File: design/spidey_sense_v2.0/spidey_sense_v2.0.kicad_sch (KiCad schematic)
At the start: 13 parts, among them J1 Input_Screw_Terminal, J2 Output_Screw_Terminal, J3 Thermocouple_Terminal, J4 Thermocouple_Terminal, J5 Thermocouple_Terminal, J6 Thermocouple_Terminal, U1 LT1025, U2 LTC1983-5

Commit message: Updated footprints
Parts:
- U1: footprint SamacSys_Parts:SOIC127P599X175-8N -> Package_SO:SOP-8_3.9x4.9mm_P1.27mm
- U2: footprint SamacSys_Parts:SOT95P280X100-6N -> Package_SO:TSOP-6_1.65x3.05mm_P0.95mm
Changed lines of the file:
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@@
     (property "Reference" "U1" (id 0) (at 80.01 70.739 0))
     (property "Value" "LT1025" (id 1) (at 80.01 73.0504 0))
-    (property "Footprint" "SamacSys_Parts:SOIC127P599X175-8N" (id 2) (at 63.5 73.66 0)
+    (property "Footprint" "Package_SO:SOP-8_3.9x4.9mm_P1.27mm" (id 2) (at 63.5 73.66 0)
       (effects (font (size 1.27 1.27)) hide)
     )
@@
     (property "Reference" "U2" (id 0) (at 143.51 28.829 0))
     (property "Value" "LTC1983-5" (id 1) (at 143.51 31.1404 0))
-    (property "Footprint" "SamacSys_Parts:SOT95P280X100-6N" (id 2) (at 143.51 39.37 0)
+    (property "Footprint" "Package_SO:TSOP-6_1.65x3.05mm_P0.95mm" (id 2) (at 143.51 39.37 0)
       (effects (font (size 1.27 1.27)) hide)
     )
@@
     )
     (path "/00000000-0000-0000-0000-000061b5397b"
-      (reference "U1") (unit 1) (value "LT1025") (footprint "SamacSys_Parts:SOIC127P599X175-8N")
+      (reference "U1") (unit 1) (value "LT1025") (footprint "Package_SO:SOP-8_3.9x4.9mm_P1.27mm")
     )
     (path "/00000000-0000-0000-0000-000061b762cd"
-      (reference "U2") (unit 1) (value "LTC1983-5") (footprint "SamacSys_Parts:SOT95P280X100-6N")
+      (reference "U2") (unit 1) (value "LTC1983-5") (footprint "Package_SO:TSOP-6_1.65x3.05mm_P0.95mm")
     )
     (path "/00000000-0000-0000-0000-000061c42e88/00000000-0000-0000-0000-000061c392ae"
-      (reference "U3") (unit 1) (value "LT1001") (footprint "SamacSys_Parts:NE555DR")
+      (reference "U3") (unit 1) (value "LT1001") (footprint "Package_SO:SOP-8_3.9x4.9mm_P1.27mm")
     )
     (path "/00000000-0000-0000-0000-000061c21e07/00000000-0000-0000-0000-000061c392ae"
-      (reference "U4") (unit 1) (value "LT1001") (footprint "SamacSys_Parts:NE555DR")
+      (reference "U4") (unit 1) (value "LT1001") (footprint "Package_SO:SOP-8_3.9x4.9mm_P1.27mm")
     )
     (path "/00000000-0000-0000-0000-000061c43179/00000000-0000-0000-0000-000061c392ae"
-      (reference "U5") (unit 1) (value "LT1001") (footprint "SamacSys_Parts:NE555DR")
+      (reference "U5") (unit 1) (value "LT1001") (footprint "Package_SO:SOP-8_3.9x4.9mm_P1.27mm")
     )
     (path "/00000000-0000-0000-0000-000061c43469/00000000-0000-0000-0000-000061c392ae"
-      (reference "U6") (unit 1) (value "LT1001") (footprint "SamacSys_Parts:NE555DR")
-    )
-  )
+      (reference "U6") (unit 1) (value "LT1001") (footprint "Package_SO:SOP-8_3.9x4.9mm_P1.27mm")
+    )
+  )

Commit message: Updated PCB
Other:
- note added: "V3"
- note added: "V4"
- note added: "V5"
- note added: "V6"
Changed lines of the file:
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@@
     (effects (font (size 1.27 1.27) (thickness 0.254) bold) (justify left bottom))
+  )
+  (text "V4" (at 223.52 78.74 0)
+    (effects (font (size 1.27 1.27)) (justify left bottom))
+  )
+  (text "V6" (at 223.52 83.82 0)
+    (effects (font (size 1.27 1.27)) (justify left bottom))
+  )
+  (text "V3" (at 223.52 76.2 0)
+    (effects (font (size 1.27 1.27)) (justify left bottom))
   )
   (text "Thermocouple Cold Junction Compensator" (at 20.32 90.17 0)
     (effects (font (size 1.27 1.27) (thickness 0.254) bold) (justify left bottom))
   )
+  (text "V5" (at 223.52 81.28 0)
+    (effects (font (size 1.27 1.27)) (justify left bottom))
+  )
   (label "K-" (at 185.42 116.84 0)

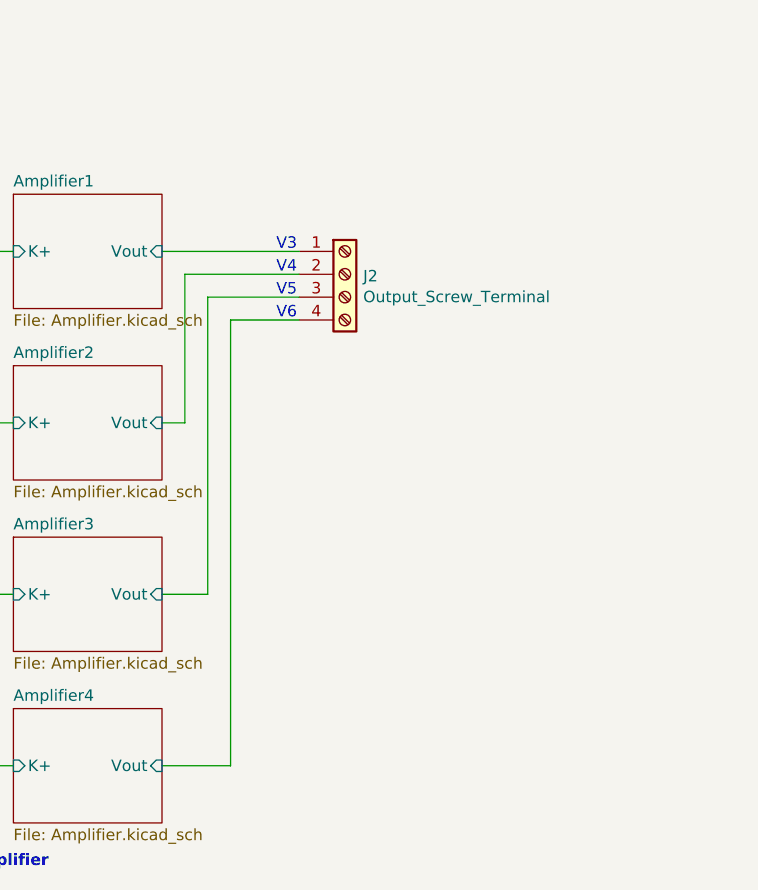
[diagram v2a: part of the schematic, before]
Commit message: Removed traces and daisy-chaining
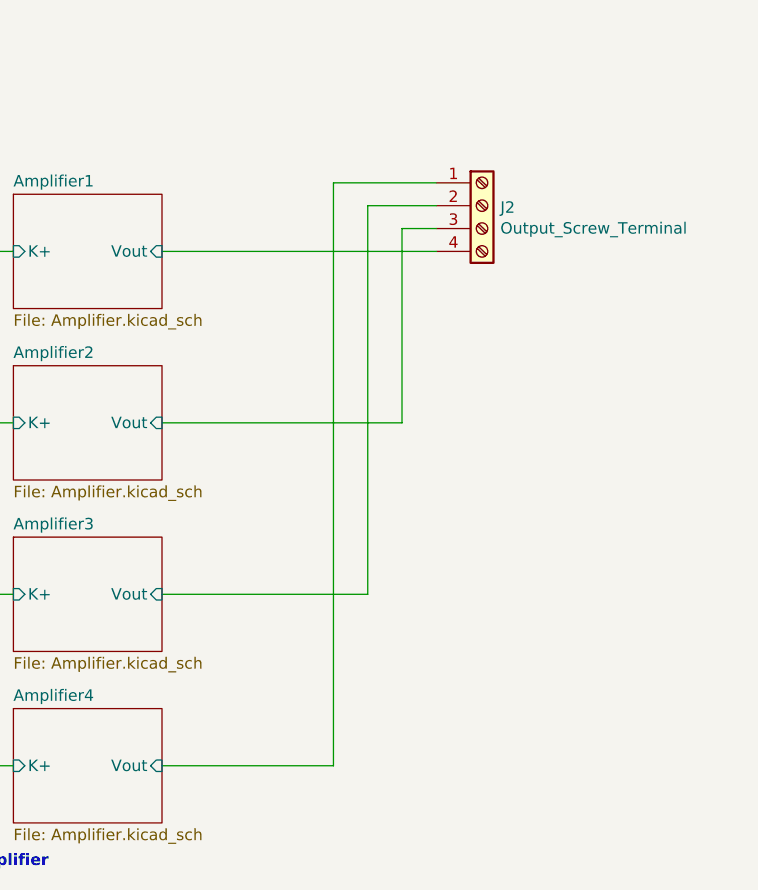
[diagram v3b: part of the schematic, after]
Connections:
- net Amplifier1/Vout: now also J2.4 (Pin_4); no longer J2.1 (Pin_1)
- net Amplifier2/Vout: now also J2.3 (Pin_3); no longer J2.2 (Pin_2)
- net Amplifier3/Vout: now also J2.2 (Pin_2); no longer J2.3 (Pin_3)
- net Amplifier4/Vout: now also J2.1 (Pin_1); no longer J2.4 (Pin_4)
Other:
- note removed: "V3"
- note removed: "V4"
- note removed: "V5"
- note removed: "V6"
- moved on the sheet: J2
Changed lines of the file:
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@@
   (no_connect (at 88.9 77.47))
   (no_connect (at 71.12 77.47))
-  (wire (pts (xy 213.36 78.74) (xy 226.06 78.74))
-    (stroke (width 0) (type default) (color 0 0 0 0))
-  )
   (wire (pts (xy 184.15 133.35) (xy 194.31 133.35))
     (stroke (width 0) (type default) (color 0 0 0 0))
   )
-  (wire (pts (xy 218.44 83.82) (xy 226.06 83.82))
-    (stroke (width 0) (type default) (color 0 0 0 0))
-  )
   (wire (pts (xy 121.92 39.37) (xy 134.62 39.37))
     (stroke (width 0) (type default) (color 0 0 0 0))
@@
     (stroke (width 0) (type default) (color 0 0 0 0))
   )
-  (wire (pts (xy 210.82 133.35) (xy 218.44 133.35))
-    (stroke (width 0) (type default) (color 0 0 0 0))
-  )
   (wire (pts (xy 127 24.13) (xy 134.62 24.13))
     (stroke (width 0) (type default) (color 0 0 0 0))
   )
-  (wire (pts (xy 213.36 95.25) (xy 213.36 78.74))
-    (stroke (width 0) (type default) (color 0 0 0 0))
-  )
-  (wire (pts (xy 210.82 76.2) (xy 226.06 76.2))
-    (stroke (width 0) (type default) (color 0 0 0 0))
-  )
   (wire (pts (xy 91.44 85.09) (xy 91.44 86.36))
     (stroke (width 0) (type default) (color 0 0 0 0))
@@
     (stroke (width 0) (type default) (color 0 0 0 0))
   )
+  (wire (pts (xy 233.68 71.12) (xy 233.68 114.3))
+    (stroke (width 0) (type default) (color 0 0 0 0))
+  )
+  (wire (pts (xy 229.87 133.35) (xy 210.82 133.35))
+    (stroke (width 0) (type default) (color 0 0 0 0))
+  )
+  (wire (pts (xy 237.49 95.25) (xy 210.82 95.25))
+    (stroke (width 0) (type default) (color 0 0 0 0))
+  )
   (wire (pts (xy 57.15 82.55) (xy 71.12 82.55))
     (stroke (width 0) (type default) (color 0 0 0 0))
@@
     (stroke (width 0) (type default) (color 0 0 0 0))
   )
-  (wire (pts (xy 218.44 83.82) (xy 218.44 133.35))
-    (stroke (width 0) (type default) (color 0 0 0 0))
-  )
   (wire (pts (xy 121.92 21.59) (xy 121.92 39.37))
     (stroke (width 0) (type default) (color 0 0 0 0))
@@
     (stroke (width 0) (type default) (color 0 0 0 0))
   )
-  (wire (pts (xy 215.9 114.3) (xy 215.9 81.28))
-    (stroke (width 0) (type default) (color 0 0 0 0))
-  )
   (wire (pts (xy 134.62 43.18) (xy 134.62 53.34))
     (stroke (width 0) (type default) (color 0 0 0 0))
   )
+  (wire (pts (xy 241.3 71.12) (xy 233.68 71.12))
+    (stroke (width 0) (type default) (color 0 0 0 0))
+  )
   (wire (pts (xy 82.55 40.64) (xy 86.36 40.64))
     (stroke (width 0) (type default) (color 0 0 0 0))
   )
-  (wire (pts (xy 210.82 114.3) (xy 215.9 114.3))
-    (stroke (width 0) (type default) (color 0 0 0 0))
-  )
   (wire (pts (xy 184.15 97.79) (xy 185.42 97.79))
     (stroke (width 0) (type default) (color 0 0 0 0))
   )
-  (wire (pts (xy 210.82 95.25) (xy 213.36 95.25))
-    (stroke (width 0) (type default) (color 0 0 0 0))
-  )
   (wire (pts (xy 57.15 81.28) (xy 57.15 82.55))
     (stroke (width 0) (type default) (color 0 0 0 0))
   )
+  (wire (pts (xy 241.3 73.66) (xy 237.49 73.66))
+    (stroke (width 0) (type default) (color 0 0 0 0))
+  )
   (wire (pts (xy 184.15 95.25) (xy 194.31 95.25))
     (stroke (width 0) (type default) (color 0 0 0 0))
@@
     (stroke (width 0) (type default) (color 0 0 0 0))
   )
+  (wire (pts (xy 210.82 76.2) (xy 241.3 76.2))
+    (stroke (width 0) (type default) (color 0 0 0 0))
+  )
+  (wire (pts (xy 233.68 114.3) (xy 210.82 114.3))
+    (stroke (width 0) (type default) (color 0 0 0 0))
+  )
+  (wire (pts (xy 229.87 68.58) (xy 229.87 133.35))
+    (stroke (width 0) (type default) (color 0 0 0 0))
+  )
   (wire (pts (xy 184.15 135.89) (xy 185.42 135.89))
     (stroke (width 0) (type default) (color 0 0 0 0))
   )
+  (wire (pts (xy 237.49 73.66) (xy 237.49 95.25))
+    (stroke (width 0) (type default) (color 0 0 0 0))
+  )
+  (wire (pts (xy 241.3 68.58) (xy 229.87 68.58))
+    (stroke (width 0) (type default) (color 0 0 0 0))
+  )
   (wire (pts (xy 152.4 24.13) (xy 152.4 35.56))
     (stroke (width 0) (type default) (color 0 0 0 0))
@@
   )
   (wire (pts (xy 82.55 43.18) (xy 86.36 43.18))
-    (stroke (width 0) (type default) (color 0 0 0 0))
-  )
-  (wire (pts (xy 215.9 81.28) (xy 226.06 81.28))
     (stroke (width 0) (type default) (color 0 0 0 0))
   )
@@
     (effects (font (size 1.27 1.27) (thickness 0.254) bold) (justify left bottom))
   )
-  (text "V4" (at 223.52 78.74 0)
-    (effects (font (size 1.27 1.27)) (justify left bottom))
-  )
-  (text "V6" (at 223.52 83.82 0)
-    (effects (font (size 1.27 1.27)) (justify left bottom))
-  )
-  (text "V3" (at 223.52 76.2 0)
-    (effects (font (size 1.27 1.27)) (justify left bottom))
-  )
   (text "Thermocouple Cold Junction Compensator" (at 20.32 90.17 0)
     (effects (font (size 1.27 1.27) (thickness 0.254) bold) (justify left bottom))
-  )
-  (text "V5" (at 223.52 81.28 0)
-    (effects (font (size 1.27 1.27)) (justify left bottom))
   )
   (label "K-" (at 185.42 116.84 0)
@@
     (pin "1")
   )
-  (symbol (lib_id "Connector:Screw_Terminal_01x04") (at 231.14 78.74 0) (unit 1)
-    (in_bom yes) (on_board yes)
-    (property "Reference" "J2" (id 0) (at 233.172 78.9432 0)
+  (symbol (lib_id "Connector:Screw_Terminal_01x04") (at 246.38 71.12 0) (unit 1)
+    (in_bom yes) (on_board yes)
+    (property "Reference" "J2" (id 0) (at 248.412 71.3232 0)
       (effects (font (size 1.27 1.27)) (justify left))
     )
-    (property "Value" "Output_Screw_Terminal" (id 1) (at 233.172 81.2546 0)
+    (property "Value" "Output_Screw_Terminal" (id 1) (at 248.412 73.6346 0)
       (effects (font (size 1.27 1.27)) (justify left))
     )
-    (property "Footprint" "TerminalBlock_Phoenix:TerminalBlock_Phoenix_MKDS-1,5-4-5.08_1x04_P5.08mm_Horizontal" (id 2) (at 231.14 78.74 0)
-      (effects (font (size 1.27 1.27)) hide)
-    )
-    (property "Datasheet" "~" (id 3) (at 231.14 78.74 0)
-      (effects (font (size 1.27 1.27)) hide)
-    )
+    (property "Footprint" "TerminalBlock_Phoenix:TerminalBlock_Phoenix_MKDS-1,5-4-5.08_1x04_P5.08mm_Horizontal" (id 2) (at 246.38 71.12 0)
+      (effects (font (size 1.27 1.27)) hide)
+    )
+    (property "Datasheet" "~" (id 3) (at 246.38 71.12 0)
+      (effects (font (size 1.27 1.27)) hide)
+    )
